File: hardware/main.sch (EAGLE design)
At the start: 94 parts, among them SW1 USER_SLIDE, SW2 USER_SLIDE, U1 TMS320F28069_PN_80, U10 TXB0101_DBV_6, U2 SN74LVC4245A_DW_24, U3 Value, U4 SN74LVC4245A_DW_24, U5 Value, U6 SN74ABT541B_DW_20, U7 SN74LVC1G04_DBV_5, U8 SST25VF080BS2AF, U9 TXB0101_DBV_6

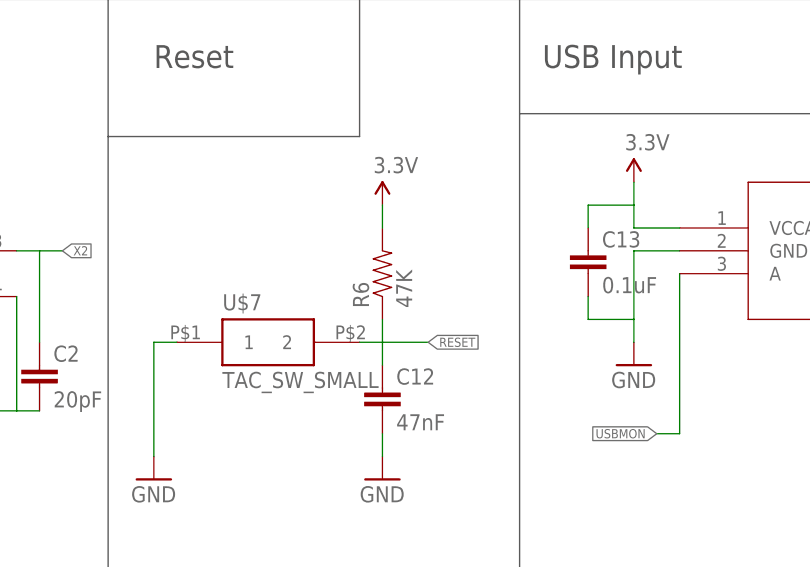
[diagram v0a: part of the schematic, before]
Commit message: Final of v1. Sent to fab house. DRC and minor silkscreen updates
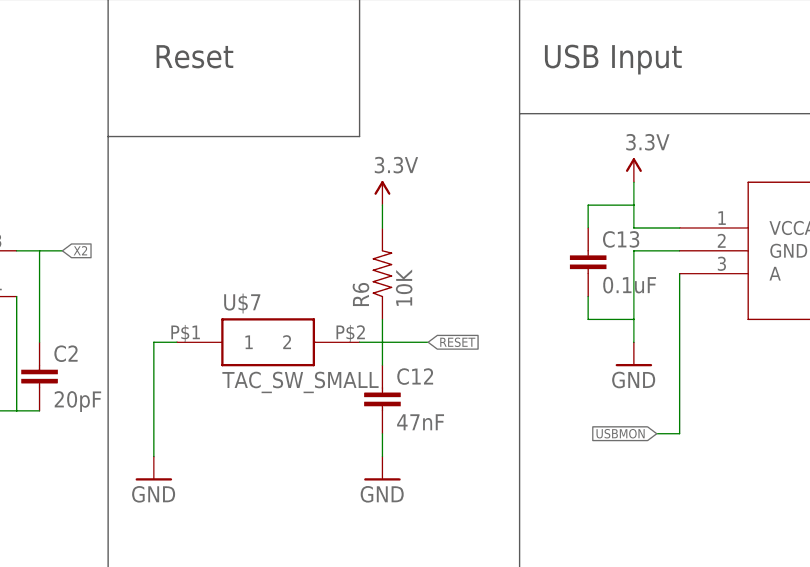
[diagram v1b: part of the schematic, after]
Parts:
- R6: value 47K -> 10K
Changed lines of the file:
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@@
 <grid distance="0.1" unitdist="inch" unit="inch" style="lines" multiple="1" display="no" altdistance="0.01" altunitdist="inch" altunit="inch"/>
 <layers>
-<layer number="1" name="Top" color="4" fill="1" visible="no" active="no"/>
-<layer number="2" name="Route2" color="1" fill="3" visible="no" active="no"/>
-<layer number="3" name="Route3" color="4" fill="3" visible="no" active="no"/>
-<layer number="4" name="Route4" color="1" fill="4" visible="no" active="no"/>
-<layer number="5" name="Route5" color="4" fill="4" visible="no" active="no"/>
-<layer number="6" name="Route6" color="1" fill="8" visible="no" active="no"/>
-<layer number="7" name="Route7" color="4" fill="8" visible="no" active="no"/>
-<layer number="8" name="Route8" color="1" fill="2" visible="no" active="no"/>
-<layer number="9" name="Route9" color="4" fill="2" visible="no" active="no"/>
-<layer number="10" name="Route10" color="1" fill="7" visible="no" active="no"/>
-<layer number="11" name="Route11" color="4" fill="7" visible="no" active="no"/>
-<layer number="12" name="Route12" color="1" fill="5" visible="no" active="no"/>
-<layer number="13" name="Route13" color="4" fill="5" visible="no" active="no"/>
-<layer number="14" name="Route14" color="1" fill="6" visible="no" active="no"/>
-<layer number="15" name="Route15" color="4" fill="6" visible="no" active="no"/>
-<layer number="16" name="Bottom" color="1" fill="1" visible="no" active="no"/>
-<layer number="17" name="Pads" color="2" fill="1" visible="no" active="no"/>
-<layer number="18" name="Vias" color="2" fill="1" visible="no" active="no"/>
-<layer number="19" name="Unrouted" color="6" fill="1" visible="no" active="no"/>
-<layer number="20" name="Dimension" color="15" fill="1" visible="no" active="no"/>
-<layer number="21" name="tPlace" color="7" fill="1" visible="no" active="no"/>
-<layer number="22" name="bPlace" color="7" fill="1" visible="no" active="no"/>
-<layer number="23" name="tOrigins" color="15" fill="1" visible="no" active="no"/>
-<layer number="24" name="bOrigins" color="15" fill="1" visible="no" active="no"/>
-<layer number="25" name="tNames" color="7" fill="1" visible="no" active="no"/>
-<layer number="26" name="bNames" color="7" fill="1" visible="no" active="no"/>
-<layer number="27" name="tValues" color="7" fill="1" visible="no" active="no"/>
-<layer number="28" name="bValues" color="7" fill="1" visible="no" active="no"/>
+<layer number="1" name="Top" color="4" fill="1" visible="yes" active="no"/>
+<layer number="2" name="Route2" color="1" fill="3" visible="yes" active="no"/>
+<layer number="3" name="Route3" color="4" fill="3" visible="yes" active="no"/>
+<layer number="4" name="Route4" color="1" fill="4" visible="yes" active="no"/>
+<layer number="5" name="Route5" color="4" fill="4" visible="yes" active="no"/>
+<layer number="6" name="Route6" color="1" fill="8" visible="yes" active="no"/>
+<layer number="7" name="Route7" color="4" fill="8" visible="yes" active="no"/>
+<layer number="8" name="Route8" color="1" fill="2" visible="yes" active="no"/>
+<layer number="9" name="Route9" color="4" fill="2" visible="yes" active="no"/>
+<layer number="10" name="Route10" color="1" fill="7" visible="yes" active="no"/>
+<layer number="11" name="Route11" color="4" fill="7" visible="yes" active="no"/>
+<layer number="12" name="Route12" color="1" fill="5" visible="yes" active="no"/>
+<layer number="13" name="Route13" color="4" fill="5" visible="yes" active="no"/>
+<layer number="14" name="Route14" color="1" fill="6" visible="yes" active="no"/>
+<layer number="15" name="Route15" color="4" fill="6" visible="yes" active="no"/>
+<layer number="16" name="Bottom" color="1" fill="1" visible="yes" active="no"/>
+<layer number="17" name="Pads" color="2" fill="1" visible="yes" active="no"/>
+<layer number="18" name="Vias" color="2" fill="1" visible="yes" active="no"/>
+<layer number="19" name="Unrouted" color="6" fill="1" visible="yes" active="no"/>
+<layer number="20" name="Dimension" color="15" fill="1" visible="yes" active="no"/>
+<layer number="21" name="tPlace" color="7" fill="1" visible="yes" active="no"/>
+<layer number="22" name="bPlace" color="7" fill="1" visible="yes" active="no"/>
+<layer number="23" name="tOrigins" color="15" fill="1" visible="yes" active="no"/>
+<layer number="24" name="bOrigins" color="15" fill="1" visible="yes" active="no"/>
+<layer number="25" name="tNames" color="7" fill="1" visible="yes" active="no"/>
+<layer number="26" name="bNames" color="7" fill="1" visible="yes" active="no"/>
+<layer number="27" name="tValues" color="7" fill="1" visible="yes" active="no"/>
+<layer number="28" name="bValues" color="7" fill="1" visible="yes" active="no"/>
 <layer number="29" name="tStop" color="7" fill="3" visible="no" active="no"/>
 <layer number="30" name="bStop" color="7" fill="6" visible="no" active="no"/>
@@
 <layer number="35" name="tGlue" color="7" fill="4" visible="no" active="no"/>
 <layer number="36" name="bGlue" color="7" fill="5" visible="no" active="no"/>
-<layer number="37" name="tTest" color="7" fill="1" visible="no" active="no"/>
-<layer number="38" name="bTest" color="7" fill="1" visible="no" active="no"/>
+<layer number="37" name="tTest" color="7" fill="1" visible="yes" active="no"/>
+<layer number="38" name="bTest" color="7" fill="1" visible="yes" active="no"/>
 <layer number="39" name="tKeepout" color="4" fill="11" visible="no" active="no"/>
 <layer number="40" name="bKeepout" color="1" fill="11" visible="no" active="no"/>
@@
 <layer number="44" name="Drills" color="7" fill="1" visible="no" active="no"/>
 <layer number="45" name="Holes" color="7" fill="1" visible="no" active="no"/>
-<layer number="46" name="Milling" color="3" fill="1" visible="no" active="no"/>
-<layer number="47" name="Measures" color="7" fill="1" visible="no" active="no"/>
-<layer number="48" name="Document" color="7" fill="1" visible="no" active="no"/>
-<layer number="49" name="Reference" color="7" fill="1" visible="no" active="no"/>
-<layer number="50" name="dxf" color="7" fill="1" visible="no" active="no"/>
-<layer number="51" name="tDocu" color="7" fill="1" visible="no" active="no"/>
-<layer number="52" name="bDocu" color="7" fill="1" visible="no" active="no"/>
-<layer number="53" name="tGND_GNDA" color="7" fill="9" visible="no" active="no"/>
-<layer number="54" name="bGND_GNDA" color="1" fill="9" visible="no" active="no"/>
-<layer number="56" name="wert" color="7" fill="1" visible="no" active="no"/>
-<layer number="57" name="tCAD" color="7" fill="1" visible="no" active="no"/>
+<layer number="46" name="Milling" color="3" fill="1" visible="yes" active="no"/>
+<layer number="47" name="Measures" color="7" fill="1" visible="yes" active="no"/>
+<layer number="48" name="Document" color="7" fill="1" visible="yes" active="no"/>
+<layer number="49" name="Reference" color="7" fill="1" visible="yes" active="no"/>
+<layer number="50" name="dxf" color="7" fill="1" visible="yes" active="no"/>
+<layer number="51" name="tDocu" color="7" fill="1" visible="yes" active="no"/>
+<layer number="52" name="bDocu" color="7" fill="1" visible="yes" active="no"/>
+<layer number="53" name="tGND_GNDA" color="7" fill="9" visible="yes" active="no"/>
+<layer number="54" name="bGND_GNDA" color="1" fill="9" visible="yes" active="no"/>
+<layer number="56" name="wert" color="7" fill="1" visible="yes" active="no"/>
+<layer number="57" name="tCAD" color="7" fill="1" visible="yes" active="no"/>
 <layer number="90" name="Modules" color="5" fill="1" visible="yes" active="yes"/>
 <layer number="91" name="Nets" color="2" fill="1" visible="yes" active="yes"/>
@@
 <part name="SUPPLY12" library="SparkFun-Aesthetics" deviceset="3.3V" device=""/>
 <part name="GND14" library="SparkFun-Aesthetics" deviceset="GND" device=""/>
-<part name="R6" library="SparkFun-Resistors" deviceset="47KOHM1/10W1%(0603)" device="" value="47K"/>
+<part name="R6" library="SparkFun-Resistors" deviceset="47KOHM1/10W1%(0603)" device="" value="10K"/>
 <part name="C12" library="SparkFun-Capacitors" deviceset="47NF(0.047UF/47000PF)-25V-5%(0603)" device="SMD" value="47nF"/>
 <part name="GND5" library="SparkFun-Aesthetics" deviceset="GND" device=""/>

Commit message: Updated connections to include nets. Fixed connection problem between VDD and VDDIO pins
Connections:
- new net VDD: C10.1, C11.1, C3.1, C6.1, C8.1, C9.1, U1.VDD, U1.VDD_2, U1.VDD_3, U1.VDD_4, U1.VDD_5, U1.VDD_6
- net 3.3V: no longer C10.1, C11.1, C3.1, C6.1, C7.1, C8.1, C9.1, U1.VDD, U1.VDD_2, U1.VDD_3, U1.VDD_4, U1.VDD_5, U1.VDD_6
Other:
- moved on the sheet: D17
